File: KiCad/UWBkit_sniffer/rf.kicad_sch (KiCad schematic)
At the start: 3 parts, among them J1 Conn_Coaxial

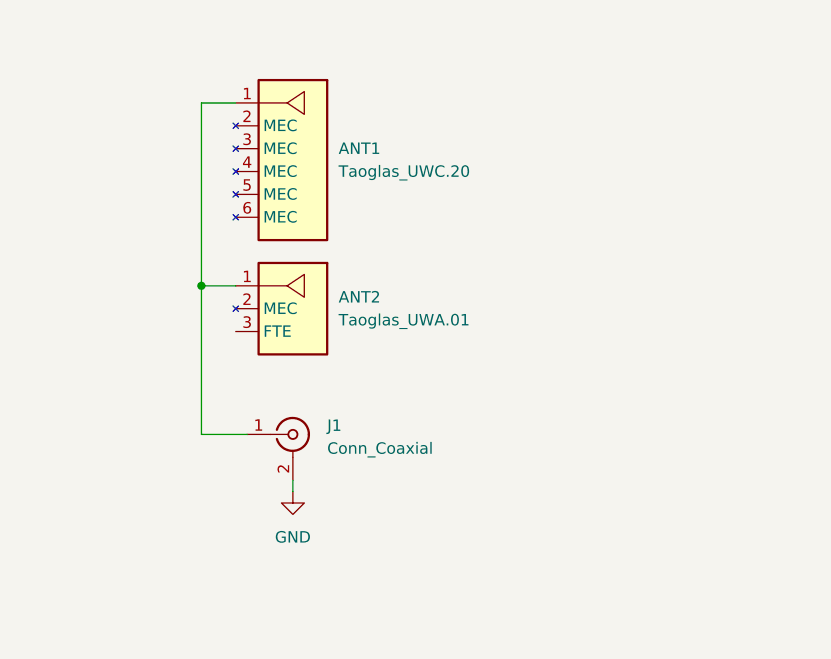
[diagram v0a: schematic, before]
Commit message: Wired connections to SoC
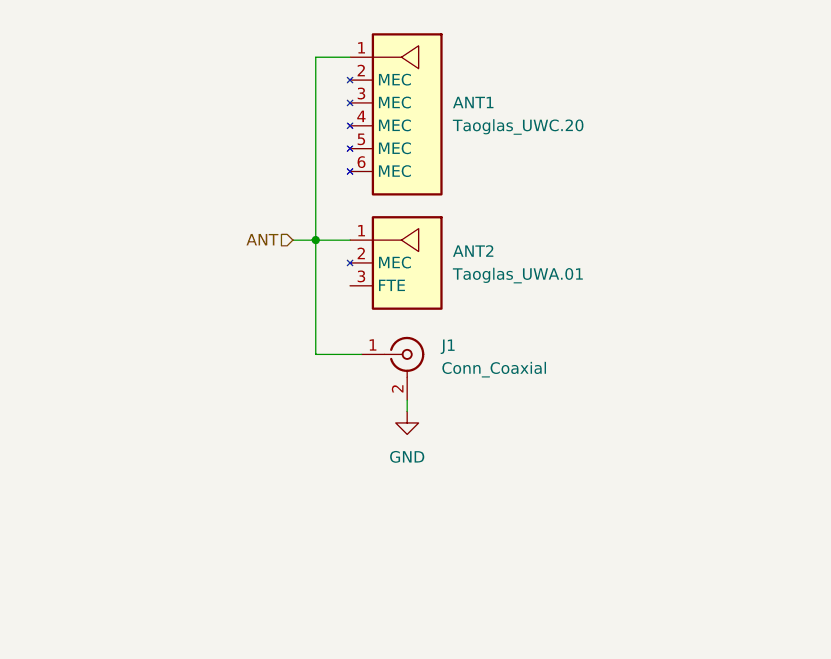
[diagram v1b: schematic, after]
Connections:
- net ANT: now reaches ANT1.1, ANT2.1, J1.1 (In)
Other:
- moved on the sheet: ANT1, ANT2, J1
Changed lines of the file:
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@@
 	(paper "A4")
 	(junction
-		(at 127 95.25)
+		(at 139.7 90.17)
 		(diameter 0)
 		(color 0 0 0 0)
@@
 	(wire
 		(pts
-			(xy 127 95.25) (xy 127 111.76)
-		)
-		(stroke
-			(width 0)
-			(type default)
-		)
-	)
-	(wire
-		(pts
-			(xy 127 74.93) (xy 127 95.25)
-		)
-		(stroke
-			(width 0)
-			(type default)
-		)
-	)
-	(wire
-		(pts
-			(xy 130.81 74.93) (xy 127 74.93)
-		)
-		(stroke
-			(width 0)
-			(type default)
-		)
-	)
-	(wire
-		(pts
-			(xy 137.16 116.84) (xy 137.16 118.11)
-		)
-		(stroke
-			(width 0)
-			(type default)
-		)
-	)
-	(wire
-		(pts
-			(xy 132.08 111.76) (xy 127 111.76)
-		)
-		(stroke
-			(width 0)
-			(type default)
-		)
-	)
-	(wire
-		(pts
-			(xy 127 95.25) (xy 130.81 95.25)
-		)
-		(stroke
-			(width 0)
-			(type default)
+			(xy 139.7 90.17) (xy 139.7 102.87)
+		)
+		(stroke
+			(width 0)
+			(type default)
+		)
+	)
+	(wire
+		(pts
+			(xy 139.7 69.85) (xy 139.7 90.17)
+		)
+		(stroke
+			(width 0)
+			(type default)
+		)
+	)
+	(wire
+		(pts
+			(xy 143.51 69.85) (xy 139.7 69.85)
+		)
+		(stroke
+			(width 0)
+			(type default)
+		)
+	)
+	(wire
+		(pts
+			(xy 149.86 107.95) (xy 149.86 109.22)
+		)
+		(stroke
+			(width 0)
+			(type default)
+		)
+	)
+	(wire
+		(pts
+			(xy 144.78 102.87) (xy 139.7 102.87)
+		)
+		(stroke
+			(width 0)
+			(type default)
+		)
+	)
+	(wire
+		(pts
+			(xy 139.7 90.17) (xy 143.51 90.17)
+		)
+		(stroke
+			(width 0)
+			(type default)
+		)
+	)
+	(wire
+		(pts
+			(xy 137.16 90.17) (xy 139.7 90.17)
+		)
+		(stroke
+			(width 0)
+			(type default)
+		)
+	)
+	(hierarchical_label "ANT"
+		(shape input)
+		(at 137.16 90.17 180)
+		(effects
+			(font
+				(size 1.27 1.27)
+			)
+			(justify right)
 		)
 	)
 	(symbol
 		(lib_id "UWB_Antennas:Taoglas_UWC.20")
-		(at 133.35 82.55 270)
+		(at 146.05 77.47 270)
 		(unit 1)
 		(exclude_from_sim no)
@@
 		(fields_autoplaced yes)
 		(property "Reference" "ANT1"
-			(at 142.24 80.0099 90)
+			(at 154.94 74.9299 90)
 			(effects
 				(font
@@
 		)
 		(property "Value" "Taoglas_UWC.20"
-			(at 142.24 82.5499 90)
+			(at 154.94 77.4699 90)
 			(effects
 				(font
@@
 		)
 		(property "Footprint" "UWB_Antennas:Taoglas_UWC.20"
-			(at 120.142 82.55 0)
+			(at 132.842 77.47 0)
 			(effects
 				(font
@@
 		)
 		(property "Datasheet" "https://www.taoglas.com/datasheets/UWC.20.pdf"
-			(at 116.586 82.55 0)
+			(at 129.286 77.47 0)
 			(effects
 				(font
@@
 		)
 		(property "Description" "3-5GHz & 6-9GHz Ultra-Wide Band (UWB) SMD Chip Antenna"
-			(at 118.11 82.55 0)
+			(at 130.81 77.47 0)
 			(effects
 				(font
@@
 	(symbol
 		(lib_id "Connector:Conn_Coaxial")
-		(at 137.16 111.76 0)
+		(at 149.86 102.87 0)
 		(unit 1)
 		(exclude_from_sim no)
@@
 		(fields_autoplaced yes)
 		(property "Reference" "J1"
-			(at 140.97 110.7831 0)
+			(at 153.67 101.8931 0)
 			(effects
 				(font
@@
 		)
 		(property "Value" "Conn_Coaxial"
-			(at 140.97 113.3231 0)
+			(at 153.67 104.4331 0)
 			(effects
 				(font
@@
 		)
 		(property "Footprint" "Connector_Coaxial:SMA_Molex_73251-1153_EdgeMount_Horizontal"
-			(at 137.16 111.76 0)
+			(at 149.86 102.87 0)
 			(effects
 				(font
@@
 		)
 		(property "Datasheet" "~"
-			(at 137.16 111.76 0)
+			(at 149.86 102.87 0)
 			(effects
 				(font
@@
 		)
 		(property "Description" "coaxial connector (BNC, SMA, SMB, SMC, Cinch/RCA, LEMO, ...)"
-			(at 137.16 111.76 0)
+			(at 149.86 102.87 0)
 			(effects
 				(font
@@
 	(symbol
 		(lib_id "UWB_Antennas:Taoglas_UWA.01")
-		(at 144.78 97.79 270)
+		(at 157.48 92.71 270)
 		(unit 1)
 		(exclude_from_sim no)
@@
 		(fields_autoplaced yes)
 		(property "Reference" "ANT2"
-			(at 142.24 96.5199 90)
+			(at 154.94 91.4399 90)
 			(effects
 				(font
@@
 		)
 		(property "Value" "Taoglas_UWA.01"
-			(at 142.24 99.0599 90)
+			(at 154.94 93.9799 90)
 			(effects
 				(font
@@
 		)
 		(property "Footprint" "UWB_Antennas:Taoglas_UWA.01"
-			(at 144.78 97.79 0)
+			(at 157.48 92.71 0)
 			(effects
 				(font
@@
 		)
 		(property "Datasheet" ""
-			(at 144.78 97.79 0)
+			(at 157.48 92.71 0)
 			(effects
 				(font
@@
 		)
 		(property "Description" "6-9GHz UWB Ceramic Substrate Chip Antenna 3.2*1.6*0.5(mm)"
-			(at 144.78 97.79 0)
+			(at 157.48 92.71 0)
 			(effects
 				(font
@@
 	(symbol
 		(lib_id "power:GND")
-		(at 137.16 118.11 0)
+		(at 149.86 109.22 0)
 		(unit 1)
 		(exclude_from_sim no)
@@
 		(fields_autoplaced yes)
 		(property "Reference" "#PWR01"
-			(at 137.16 124.46 0)
+			(at 149.86 115.57 0)
 			(effects
 				(font
@@
 		)
 		(property "Value" "GND"
-			(at 137.16 123.19 0)
+			(at 149.86 114.3 0)
 			(effects
 				(font
@@
 		)
 		(property "Footprint" ""
-			(at 137.16 118.11 0)
+			(at 149.86 109.22 0)
 			(effects
 				(font
@@
 		)
 		(property "Datasheet" ""
-			(at 137.16 118.11 0)
+			(at 149.86 109.22 0)
 			(effects
 				(font
@@
 		)
 		(property "Description" "Power symbol creates a global label with name \"GND\" , ground"
-			(at 137.16 118.11 0)
-			(effects
-				(font
+			(at 149.86 109.22 0)
+			(effects
+				(font

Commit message: Added components to schematic
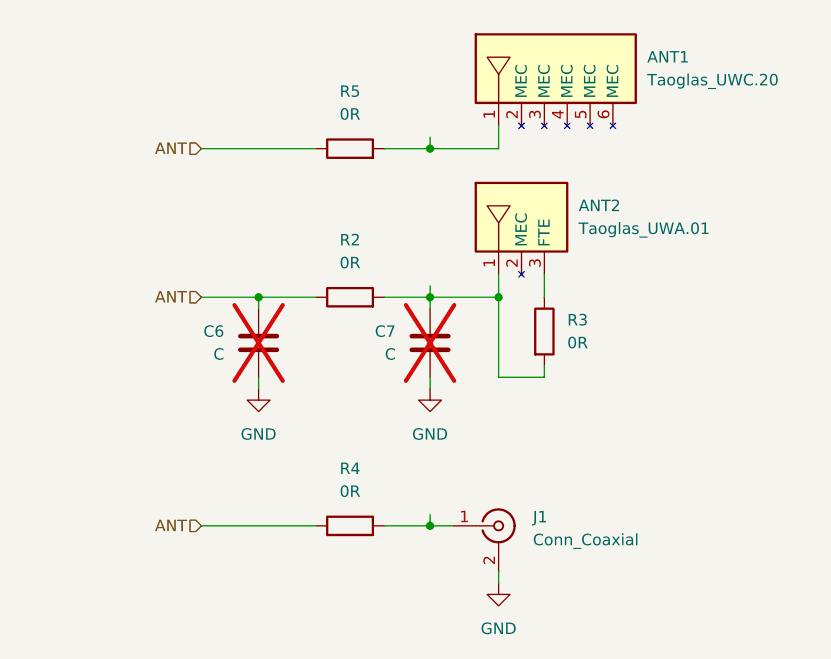
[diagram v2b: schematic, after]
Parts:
- added C6, C7: C, Capacitor_SMD:C_0603_1608Metric, symbol Device:C
- added R2, R4, R5: 0R, Resistor_SMD:R_0603_1608Metric, symbol Device:R
- added R3: 0R, Resistor_SMD:R_0402_1005Metric, symbol Device:R
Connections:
- net ANT: now also C6.1, R2.1, R4.1, R5.1; no longer ANT1.1, ANT2.1, J1.1 (In)
- net GND: now also C6.2, C7.2
- net at ANT2.3 (FTE): now also R3.1
- new net: ANT2.1, C7.1, R2.2, R3.2
- new net: ANT1.1, R5.2
- new net: J1.1 (In), R4.2
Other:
- moved on the sheet: ANT1, ANT2, J1

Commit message: First version of PCB
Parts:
- added R12: 0R, Resistor_SMD:R_0402_1005Metric, symbol Device:R
- C6, C7: footprint Capacitor_SMD:C_0603_1608Metric -> Capacitor_SMD:C_0402_1005Metric
- R2, R4: footprint Resistor_SMD:R_0603_1608Metric -> Resistor_SMD:R_0402_1005Metric
- R3: now not fitted
- R5: footprint Resistor_SMD:R_0603_1608Metric -> Resistor_SMD:R_0402_1005Metric; now not fitted
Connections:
- net ANT: now also R12.1; no longer C6.1, R4.1
- net at ANT2.1, C7.1, R3.2: now also R4.2; no longer R2.2
- net at R5.2: now also J1.1 (In); no longer ANT1.1
- new net: ANT1.1, R2.2
- new net: C6.1, R12.2, R4.1
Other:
- note added: "Used to disconnect elements"
- moved on the sheet: C6, C7, R2

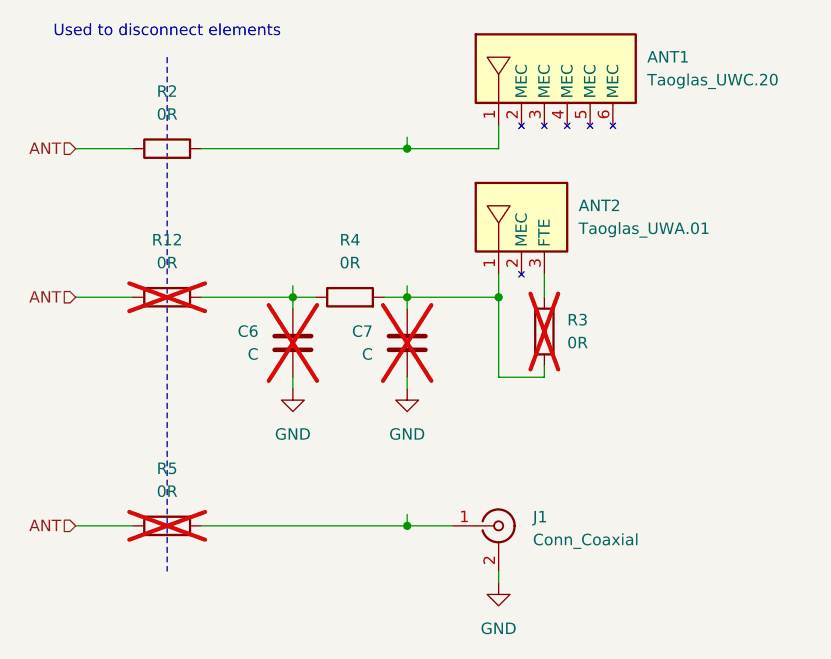
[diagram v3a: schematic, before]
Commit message: United 5V rails, modified layout of connectors
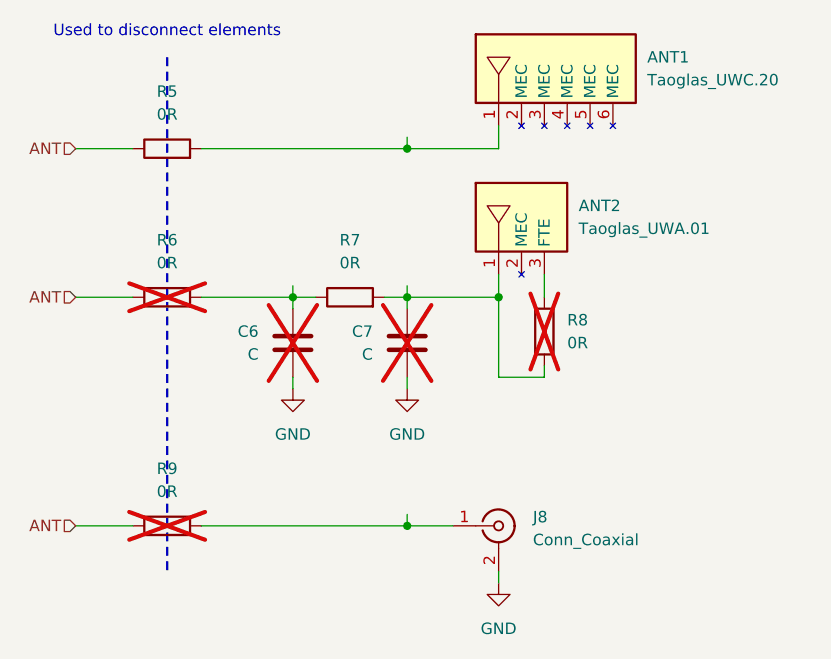
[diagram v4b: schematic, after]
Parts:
- renumbered J1 to J8, R2 to R5, R12 to R6, R4 to R7, R3 to R8, R5 to R9
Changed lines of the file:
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@@
 		)
 		(stroke
-			(width 0)
+			(width 0.25)
 			(type dash)
 			(color 255 0 0 1)
@@
 		(dnp yes)
 		(fields_autoplaced yes)
-		(property "Reference" "R5"
+		(property "Reference" "R9"
 			(at 123.19 115.57 90)
 			(effects
@@
 			(project "UWBkit_sniffer"
 				(path "/7666dc1a-7b28-48ea-a5e3-eea89f700cea/9c5400f6-8843-4efe-8f66-82919aa03da0"
-					(reference "R5")
+					(reference "R9")
 					(unit 1)
 				)
@@
 		(dnp no)
 		(fields_autoplaced yes)
-		(property "Reference" "R2"
+		(property "Reference" "R5"
 			(at 123.19 73.66 90)
 			(effects
@@
 			(project "UWBkit_sniffer"
 				(path "/7666dc1a-7b28-48ea-a5e3-eea89f700cea/9c5400f6-8843-4efe-8f66-82919aa03da0"
-					(reference "R2")
+					(reference "R5")
 					(unit 1)
 				)
@@
 		(dnp yes)
 		(fields_autoplaced yes)
-		(property "Reference" "R3"
+		(property "Reference" "R8"
 			(at 167.64 99.0599 0)
 			(effects
@@
 			(project ""
 				(path "/7666dc1a-7b28-48ea-a5e3-eea89f700cea/9c5400f6-8843-4efe-8f66-82919aa03da0"
-					(reference "R3")
+					(reference "R8")
 					(unit 1)
 				)
@@
 		(dnp no)
 		(fields_autoplaced yes)
-		(property "Reference" "J1"
+		(property "Reference" "J8"
 			(at 163.83 120.9431 0)
 			(effects
@@
 			(project "UWBkit_sniffer"
 				(path "/7666dc1a-7b28-48ea-a5e3-eea89f700cea/9c5400f6-8843-4efe-8f66-82919aa03da0"
-					(reference "J1")
+					(reference "J8")
 					(unit 1)
 				)
@@
 		(dnp no)
 		(fields_autoplaced yes)
-		(property "Reference" "#PWR010"
+		(property "Reference" "#PWR045"
 			(at 149.86 113.03 0)
 			(effects
@@
 			(project ""
 				(path "/7666dc1a-7b28-48ea-a5e3-eea89f700cea/9c5400f6-8843-4efe-8f66-82919aa03da0"
-					(reference "#PWR010")
+					(reference "#PWR045")
 					(unit 1)
 				)
@@
 		(dnp no)
 		(fields_autoplaced yes)
-		(property "Reference" "#PWR01"
+		(property "Reference" "#PWR046"
 			(at 160.02 134.62 0)
 			(effects
@@
 			(project "UWBkit_sniffer"
 				(path "/7666dc1a-7b28-48ea-a5e3-eea89f700cea/9c5400f6-8843-4efe-8f66-82919aa03da0"
-					(reference "#PWR01")
+					(reference "#PWR046")
 					(unit 1)
 				)
@@
 		(dnp yes)
 		(fields_autoplaced yes)
-		(property "Reference" "R12"
+		(property "Reference" "R6"
 			(at 123.19 90.17 90)
 			(effects
@@
 			(project "UWBkit_sniffer"
 				(path "/7666dc1a-7b28-48ea-a5e3-eea89f700cea/9c5400f6-8843-4efe-8f66-82919aa03da0"
-					(reference "R12")
+					(reference "R6")
 					(unit 1)
 				)
@@
 		(dnp no)
 		(fields_autoplaced yes)
-		(property "Reference" "#PWR012"
+		(property "Reference" "#PWR044"
 			(at 137.16 113.03 0)
 			(effects
@@
 			(project "UWBkit_sniffer"
 				(path "/7666dc1a-7b28-48ea-a5e3-eea89f700cea/9c5400f6-8843-4efe-8f66-82919aa03da0"
-					(reference "#PWR012")
+					(reference "#PWR044")
 					(unit 1)
 				)
@@
 		(dnp no)
 		(fields_autoplaced yes)
-		(property "Reference" "R4"
+		(property "Reference" "R7"
 			(at 143.51 90.17 90)
 			(effects
@@
 			(project "UWBkit_sniffer"
 				(path "/7666dc1a-7b28-48ea-a5e3-eea89f700cea/9c5400f6-8843-4efe-8f66-82919aa03da0"
-					(reference "R4")
-					(unit 1)
-				)
+					(reference "R7")
+					(unit 1)
+				)

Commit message: Removed UWA.01, added CTS/RTS connections
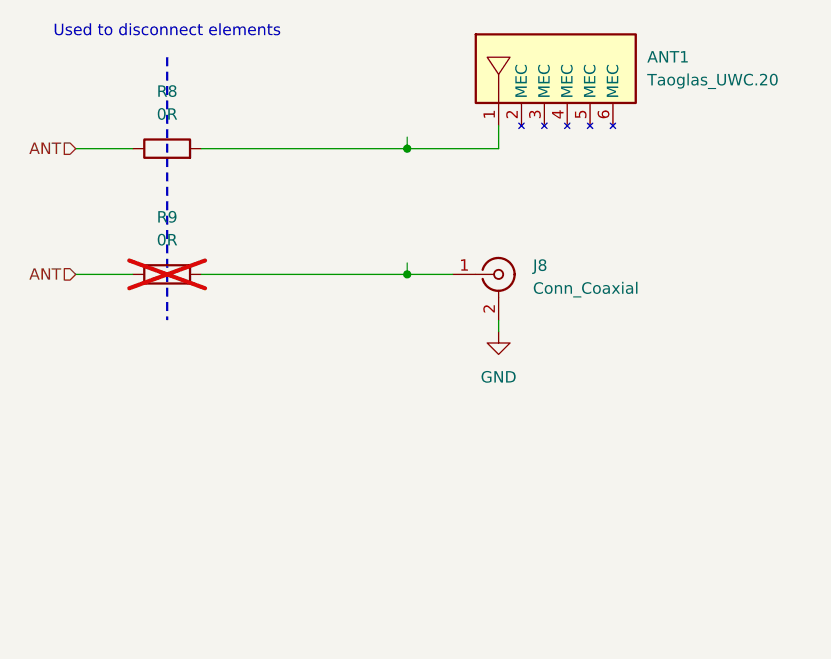
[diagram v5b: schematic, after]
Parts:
- removed ANT2: Taoglas_UWA.01, UWB_Antennas:Taoglas_UWA.01, symbol UWB_Antennas:Taoglas_UWA.01
- removed C6, C7: C, Capacitor_SMD:C_0402_1005Metric, symbol Device:C
- removed R6, R7, R8: 0R, Resistor_SMD:R_0402_1005Metric, symbol Device:R
- renumbered R5 to R8
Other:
- moved on the sheet: J8, R9

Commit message: Redone RF trace, repositioned UWC.20 and mounting holes
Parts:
- R8, R9: footprint Resistor_SMD:R_0402_1005Metric -> Resistor_SMD:R_0603_1608Metric
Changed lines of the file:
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@@
 			)
 		)
-		(property "Footprint" "Resistor_SMD:R_0402_1005Metric"
+		(property "Footprint" "Resistor_SMD:R_0603_1608Metric"
 			(at 123.19 95.758 90)
 			(effects
@@
 			)
 		)
-		(property "Footprint" "Resistor_SMD:R_0402_1005Metric"
+		(property "Footprint" "Resistor_SMD:R_0603_1608Metric"
 			(at 123.19 81.788 90)
 			(effects

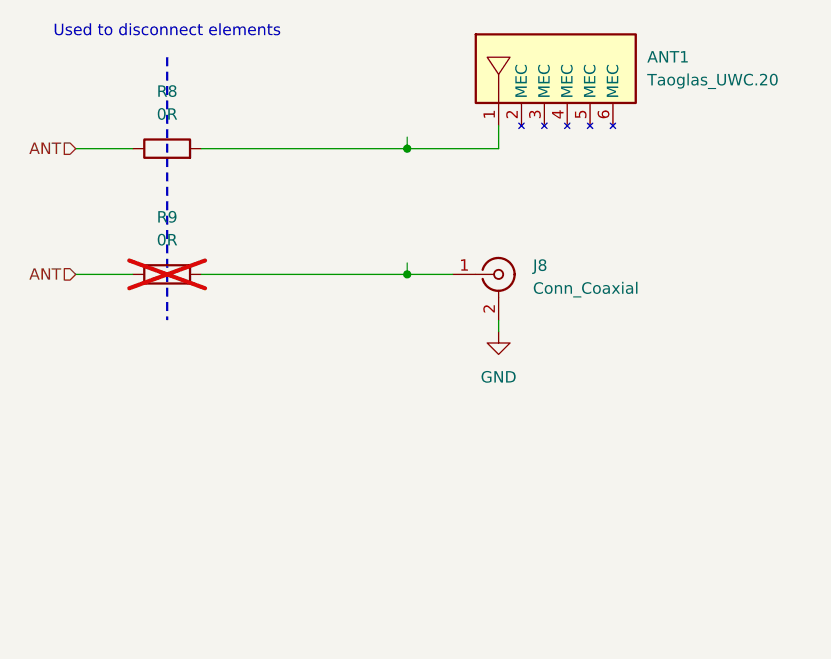
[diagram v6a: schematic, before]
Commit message: Moved pi-filter past R8 shorting resistor
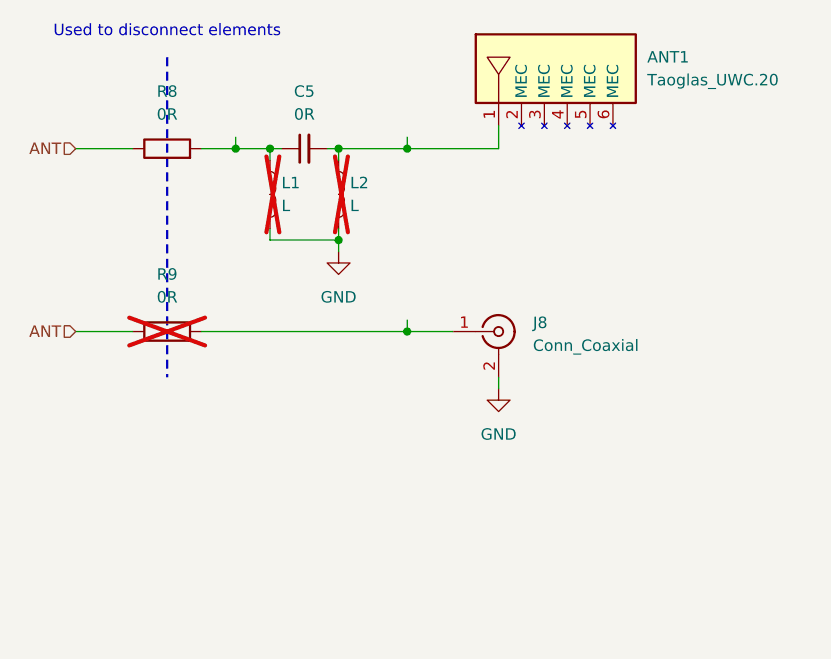
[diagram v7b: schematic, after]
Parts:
- added C5: 0R, Capacitor_SMD:C_0603_1608Metric, symbol Device:C_Small
- added L1, L2: L, Inductor_SMD:L_0603_1608Metric, symbol Device:L
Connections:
- net GND: now also L1.2, L2.2
- net at R8.2: now also C5.1, L1.1; no longer ANT1.1
- new net: ANT1.1, C5.2, L2.1
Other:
- moved on the sheet: J8, R9

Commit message: Release V1.0
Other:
- title: (none) -> RF
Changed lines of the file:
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@@
 	(generator_version "9.0")
 	(paper "A4")
+	(title_block
+		(title "RF")
+		(date "2026-02-24")
+		(rev "1.0")
+	)
 	(text "Used to disconnect elements"
 		(exclude_from_sim no)
